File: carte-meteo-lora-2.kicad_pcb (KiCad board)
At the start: 4 copper layers, 50 x 50 mm, 79 parts, among them J1 USB_C_Receptacle_USB2.0_14P, J2 Conn_Coaxial, J3 Conn_Coaxial, J4 Conn_Coaxial, J5 Conn_01x04_Pin, SW1 SW_Push, SW2 SW_Push, U1 HS96L03W2C03, U2 SX1262TR8-GC, U3 LDL212PV33R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

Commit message: pcb: add uart routing
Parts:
- moved J5 7.89 mm to (128.8, 43.7), turned to 0 degrees
- moved R15 0.75 mm to (127.0, 40.2), turned to 90 degrees
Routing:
- net Net-(J5-Pin_4): track 0.00 -> 12.0 mm
- net /U0RXD: track 0.00 -> 10.6 mm
- net /U0TXD: track 0.00 -> 2.48 mm
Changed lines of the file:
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@@
 	(footprint "Resistor_SMD:R_0402_1005Metric"
 		(layer "F.Cu")
-		(at 126.975 41 180)
+		(at 126.975 40.25 90)
 		(descr "Resistor SMD 0402 (1005 Metric), square (rectangular) end terminal, IPC-7351 nominal, (Body size source: IPC-SM-782 page 72, https://www.pcb-3d.com/wordpress/wp-content/uploads/ipc-sm-782a_amendment_1_and_2.pdf)")
 		(tags "resistor")
 		(property "Reference" "R15"
-			(at 0 -1.17 0)
+			(at 0 -1.17 90)
 			(layer "F.SilkS")
 			(effects
@@
 		)
 		(property "Value" "470"
-			(at 0 1.17 0)
+			(at 0 1.17 90)
 			(layer "F.Fab")
 			(effects
@@
 		)
 		(property "Datasheet" ""
-			(at 0 0 0)
+			(at 0 0 90)
 			(layer "F.Fab")
 			(hide yes)
@@
 		)
 		(property "Description" "Resistor"
-			(at 0 0 0)
+			(at 0 0 90)
 			(layer "F.Fab")
 			(hide yes)
@@
 		)
 		(property "KiLib_Generator" "SMD_2terminal_chip_molded"
-			(at 0 0 0)
+			(at 0 0 90)
 			(layer "F.SilkS")
 			(hide yes)
@@
 		)
 		(property "Basic" "Y"
-			(at 0 0 180)
+			(at 0 0 90)
 			(unlocked yes)
 			(layer "F.Fab")
@@
 		)
 		(property "JLCPCB Part #" "C25117"
-			(at 0 0 180)
+			(at 0 0 90)
 			(unlocked yes)
 			(layer "F.Fab")
@@
 		)
 		(property "Manufacturer" "Uniroyal Elec"
-			(at 0 0 180)
+			(at 0 0 90)
 			(unlocked yes)
 			(layer "F.Fab")
@@
 		)
 		(property "Manufacturer Part Number" "0402WGF4700TCE"
-			(at 0 0 180)
+			(at 0 0 90)
 			(unlocked yes)
 			(layer "F.Fab")
@@
 		(duplicate_pad_numbers_are_jumpers no)
 		(fp_line
-			(start -0.153641 0.38)
-			(end 0.153641 0.38)
+			(start -0.153641 -0.38)
+			(end 0.153641 -0.38)
 			(stroke
 				(width 0.12)
@@
 		)
 		(fp_line
-			(start -0.153641 -0.38)
-			(end 0.153641 -0.38)
+			(start -0.153641 0.38)
+			(end 0.153641 0.38)
 			(stroke
 				(width 0.12)
@@
 		)
 		(fp_text user "${REFERENCE}"
-			(at 0 0 0)
+			(at 0 0 90)
 			(layer "F.Fab")
 			(effects
@@
 		)
 		(pad "1" smd roundrect
-			(at -0.51 0 180)
+			(at -0.51 0 90)
 			(size 0.54 0.64)
 			(layers "F.Cu" "F.Mask" "F.Paste")
@@
 		)
 		(pad "2" smd roundrect
-			(at 0.51 0 180)
+			(at 0.51 0 90)
 			(size 0.54 0.64)
 			(layers "F.Cu" "F.Mask" "F.Paste")
@@
 	(footprint "Connector_PinHeader_2.54mm:PinHeader_1x04_P2.54mm_Vertical"
 		(layer "F.Cu")
-		(at 128.75 51.56 180)
+		(at 128.75 43.67)
 		(descr "Through hole straight pin header, 1x04, 2.54mm pitch, single row")
 		(tags "Through hole pin header THT 1x04 2.54mm single row")
@@
 		(duplicate_pad_numbers_are_jumpers no)
 		(fp_line
-			(start 1.38 1.27)
-			(end 1.38 9)
+			(start -1.38 -1.38)
+			(end 0 -1.38)
 			(stroke
 				(width 0.12)
@@
 		)
 		(fp_line
-			(start -1.38 9)
-			(end 1.38 9)
+			(start -1.38 0)
+			(end -1.38 -1.38)
 			(stroke
 				(width 0.12)
@@
 		(fp_line
 			(start -1.38 1.27)
-			(end 1.38 1.27)
+			(end -1.38 9)
 			(stroke
 				(width 0.12)
@@
 		(fp_line
 			(start -1.38 1.27)
-			(end -1.38 9)
+			(end 1.38 1.27)
 			(stroke
 				(width 0.12)
@@
 		)
 		(fp_line
-			(start -1.38 0)
-			(end -1.38 -1.38)
+			(start -1.38 9)
+			(end 1.38 9)
 			(stroke
 				(width 0.12)
@@
 		)
 		(fp_line
-			(start -1.38 -1.38)
-			(end 0 -1.38)
+			(start 1.38 1.27)
+			(end 1.38 9)
 			(stroke
 				(width 0.12)
@@
 		)
 		(fp_line
-			(start 1.27 8.89)
-			(end -1.27 8.89)
+			(start -1.27 -0.635)
+			(end -0.635 -1.27)
 			(stroke
 				(width 0.1)
@@
 		)
 		(fp_line
-			(start 1.27 -1.27)
-			(end 1.27 8.89)
+			(start -1.27 8.89)
+			(end -1.27 -0.635)
 			(stroke
 				(width 0.1)
@@
 		)
 		(fp_line
-			(start -1.27 8.89)
-			(end -1.27 -0.635)
+			(start 1.27 -1.27)
+			(end 1.27 8.89)
 			(stroke
 				(width 0.1)
@@
 		)
 		(fp_line
-			(start -1.27 -0.635)
-			(end -0.635 -1.27)
+			(start 1.27 8.89)
+			(end -1.27 8.89)
 			(stroke
 				(width 0.1)
@@
 		)
 		(pad "1" thru_hole rect
-			(at 0 0 180)
+			(at 0 0)
 			(size 1.7 1.7)
 			(drill 1)
@@
 		)
 		(pad "2" thru_hole circle
-			(at 0 2.54 180)
+			(at 0 2.54)
 			(size 1.7 1.7)
 			(drill 1)
@@
 		)
 		(pad "3" thru_hole circle
-			(at 0 5.08 180)
+			(at 0 5.08)
 			(size 1.7 1.7)
 			(drill 1)
@@
 		)
 		(pad "4" thru_hole circle
-			(at 0 7.62 180)
+			(at 0 7.62)
 			(size 1.7 1.7)
 			(drill 1)
@@
 	)
 	(segment
+		(start 127.54 51.29)
+		(end 126.975 50.725)
+		(width 0.2)
+		(layer "F.Cu")
+		(net "Net-(J5-Pin_4)")
+	)
+	(segment
+		(start 128.75 51.29)
+		(end 127.54 51.29)
+		(width 0.2)
+		(layer "F.Cu")
+		(net "Net-(J5-Pin_4)")
+	)
+	(segment
+		(start 126.975 50.725)
+		(end 126.975 40.76)
+		(width 0.2)
+		(layer "F.Cu")
+		(net "Net-(J5-Pin_4)")
+	)
+	(segment
+		(start 126.49 39.74)
+		(end 125.4 38.65)
+		(width 0.2)
+		(layer "F.Cu")
+		(net "/U0TXD")
+	)
+	(segment
+		(start 126.975 39.74)
+		(end 126.49 39.74)
+		(width 0.2)
+		(layer "F.Cu")
+		(net "/U0TXD")
+	)
+	(segment
+		(start 125.4 38.65)
+		(end 124.95 38.65)
+		(width 0.2)
+		(layer "F.Cu")
+		(net "/U0TXD")
+	)
+	(segment
+		(start 127.25 38.75)
+		(end 127.545 39.045)
+		(width 0.2)
+		(layer "F.Cu")
+		(net "/U0RXD")
+	)
+	(segment
+		(start 124.95 38.25)
+		(end 125.75 38.25)
+		(width 0.2)
+		(layer "F.Cu")
+		(net "/U0RXD")
+	)
+	(segment
+		(start 127.545 39.045)
+		(end 127.545 45.005)
+		(width 0.2)
+		(layer "F.Cu")
+		(net "/U0RXD")
+	)
+	(segment
+		(start 126.25 38.75)
+		(end 127.25 38.75)
+		(width 0.2)
+		(layer "F.Cu")
+		(net "/U0RXD")
+	)
+	(segment
+		(start 125.75 38.25)
+		(end 126.25 38.75)
+		(width 0.2)
+		(layer "F.Cu")
+		(net "/U0RXD")
+	)
+	(segment
+		(start 127.545 45.005)
+		(end 128.75 46.21)
+		(width 0.2)
+		(layer "F.Cu")
+		(net "/U0RXD")
+	)
+	(segment

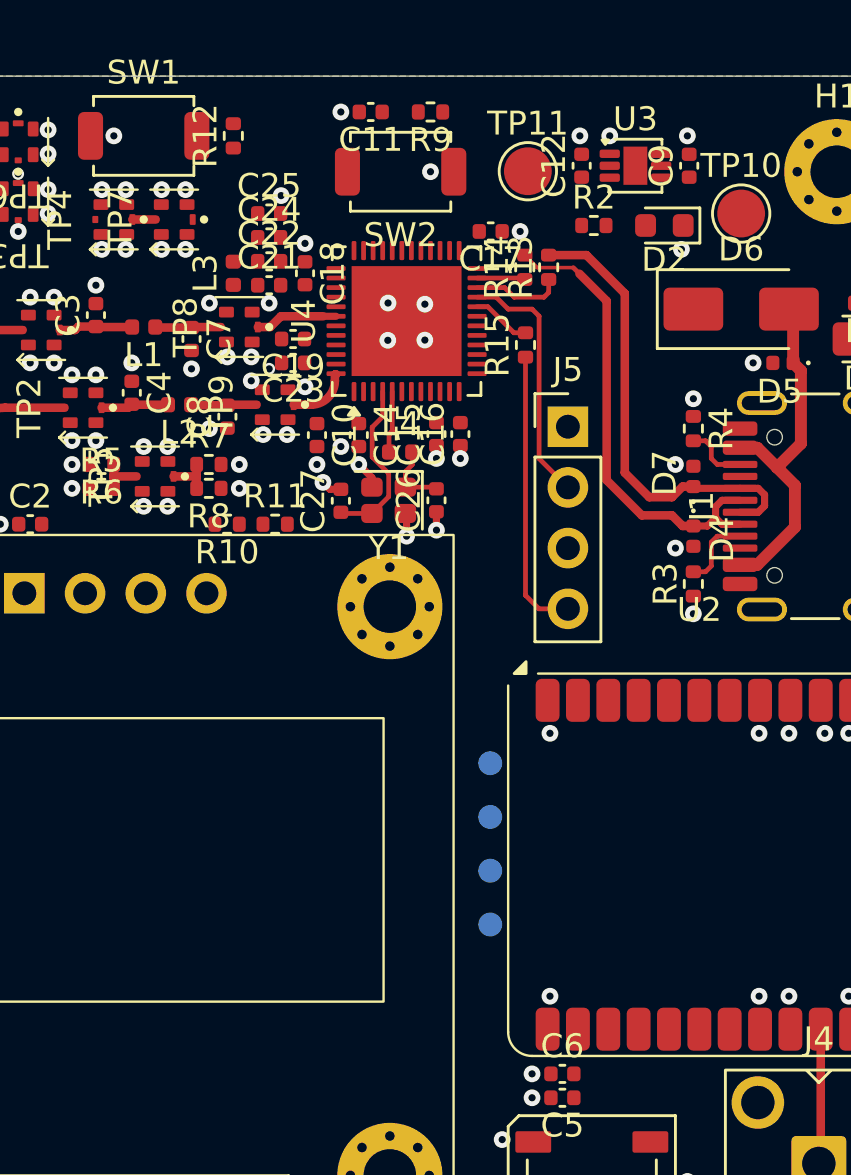
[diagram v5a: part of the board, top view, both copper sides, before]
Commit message: pcb: add i2c routing
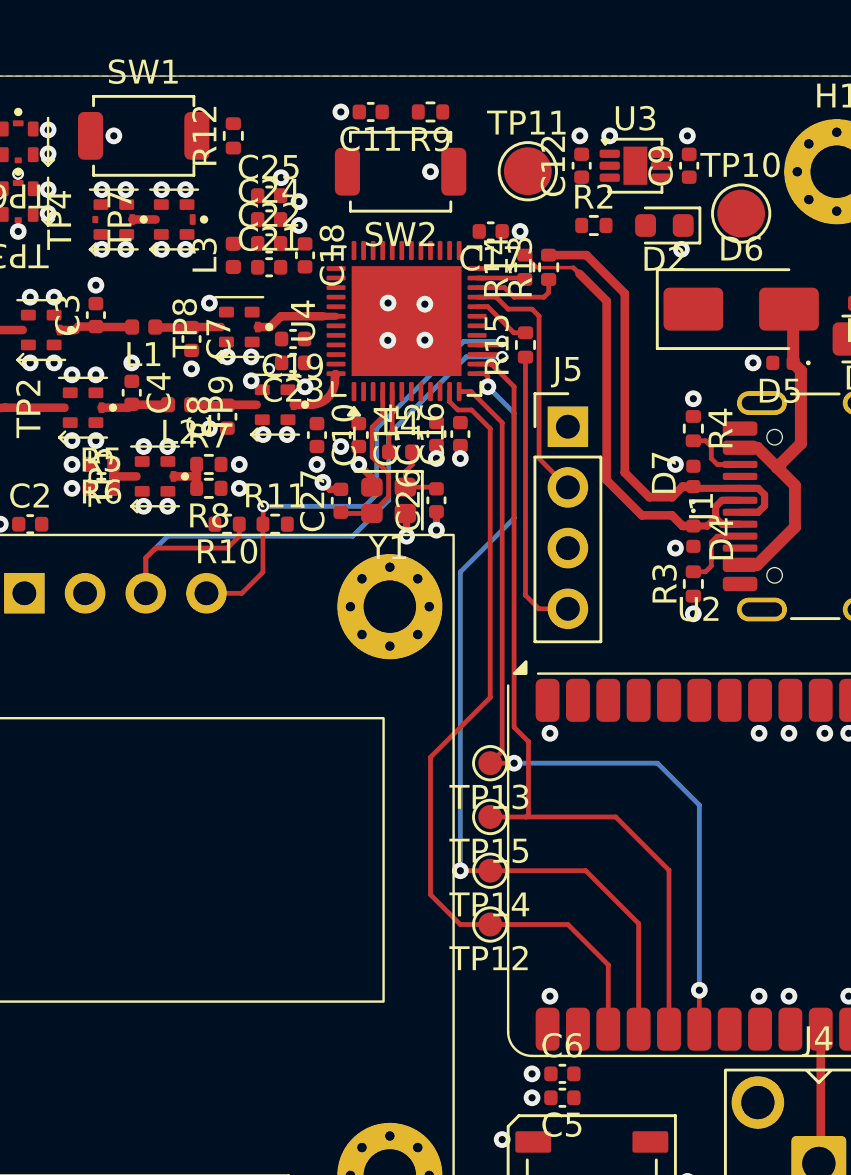
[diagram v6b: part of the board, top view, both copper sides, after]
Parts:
- TP12, TP13, TP14, TP15: moved to F.Cu
- moved C18 0.75 mm to (117.8, 36.5)
- moved C21 0.75 mm to (116.2, 37.0)
- moved C22 0.75 mm to (116.2, 36.0)
- moved C24 0.75 mm to (116.2, 35.0)
- moved C25 0.75 mm to (116.2, 34.0)
- moved L3 0.75 mm to (114.8, 36.5)
- turned TP12 to 180 degrees
- turned TP13 to 180 degrees
- turned TP14 to 180 degrees
- turned TP15 to 180 degrees
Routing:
- net /CS: track 0.00 -> 35.7 mm, vias 0 -> 2
- net /MISO: track 0.00 -> 35.4 mm, vias 0 -> 2
- net /MOSI: track 0.00 -> 35.3 mm
- net /SCK: track 0.00 -> 34.5 mm
- net /SCL: track 0.00 -> 28.8 mm, vias 0 -> 1
- net /SDA: track 0.00 -> 21.1 mm, vias 0 -> 2

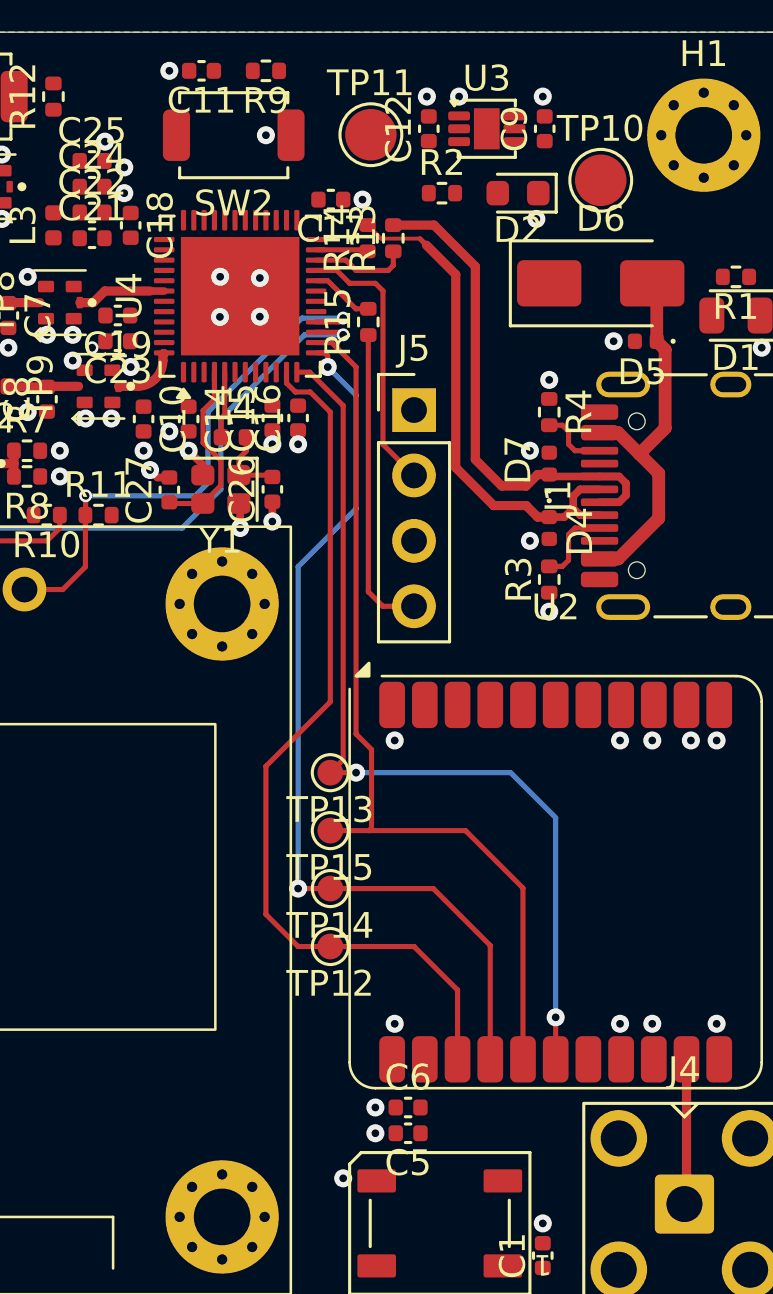
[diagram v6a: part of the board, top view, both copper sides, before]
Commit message: pcb: add lora module routing
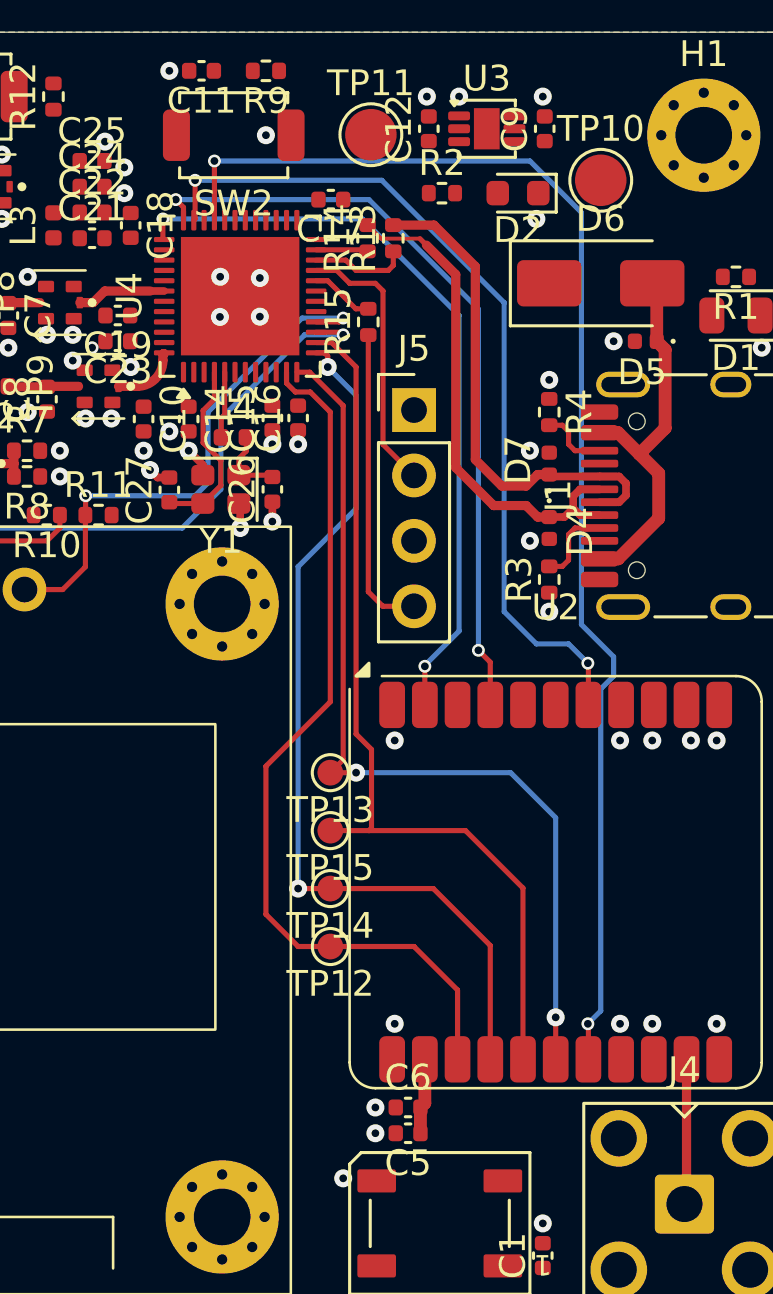
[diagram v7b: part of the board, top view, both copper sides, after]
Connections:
- U4 pad 17: /BUSY -> unconnected-(U4-GPIO8/SDIO_DATA0-Pad17)
- U4 pad 18: /DIO3 -> unconnected-(U4-GPIO9/SDIO_CLK-Pad18)
- U4 pad 19: /DIO1 -> unconnected-(U4-GPIO10/SDIO_CMD-Pad19)
- U4 pad 35: unconnected-(U4-GPIO25-Pad35) -> /DIO1
- U4 pad 36: unconnected-(U4-GPIO26-Pad36) -> /DIO3
- U4 pad 37: unconnected-(U4-GPIO27-Pad37) -> /BUSY
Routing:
- net /RST: track 0.00 -> 51.2 mm, vias 0 -> 2
- net /DIO1: track 0.00 -> 33.2 mm, vias 0 -> 2
- net /DIO3: track 0.00 -> 30.0 mm, vias 0 -> 2
- net /BUSY: track 0.00 -> 29.5 mm, vias 0 -> 2
- net +3V3: track 0.00 -> 2.94 mm
- net GND: vias 89 -> 88

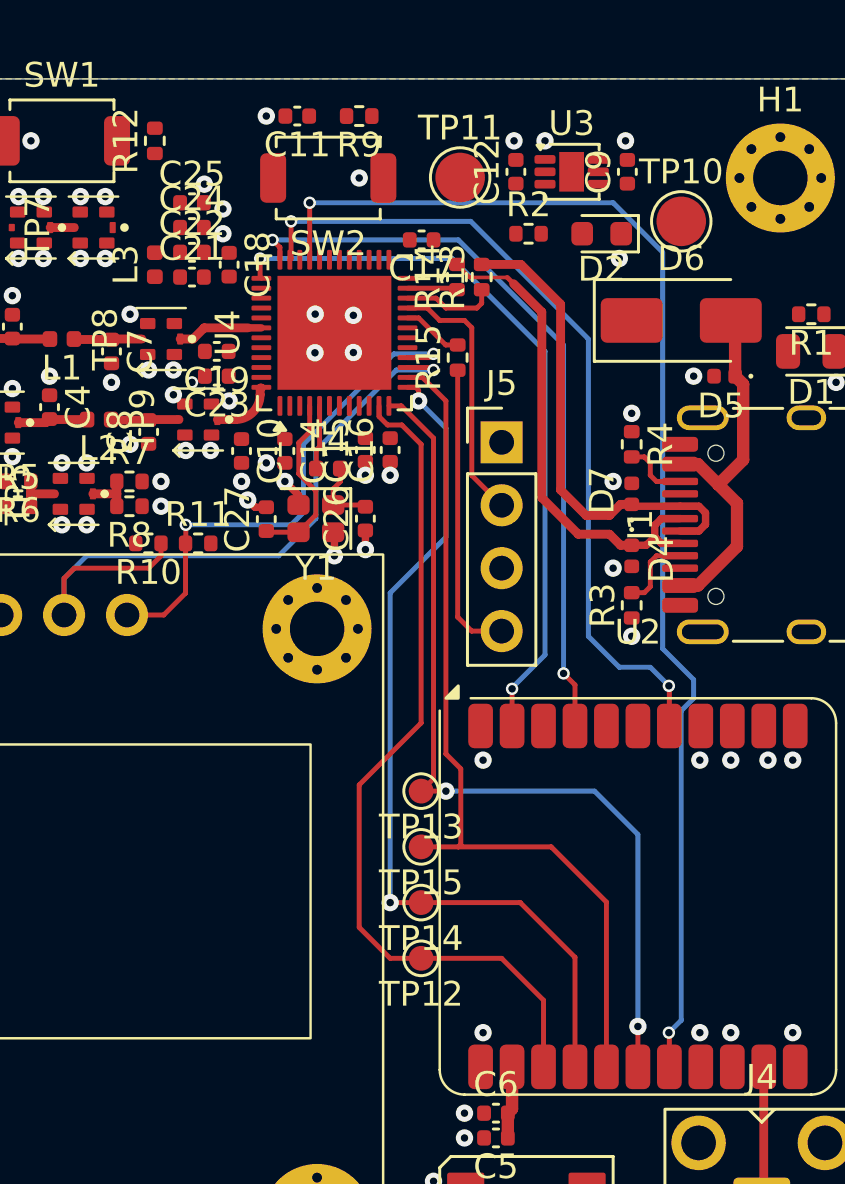
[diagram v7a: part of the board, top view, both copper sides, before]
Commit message: pcb: add +3v3 pwr routing
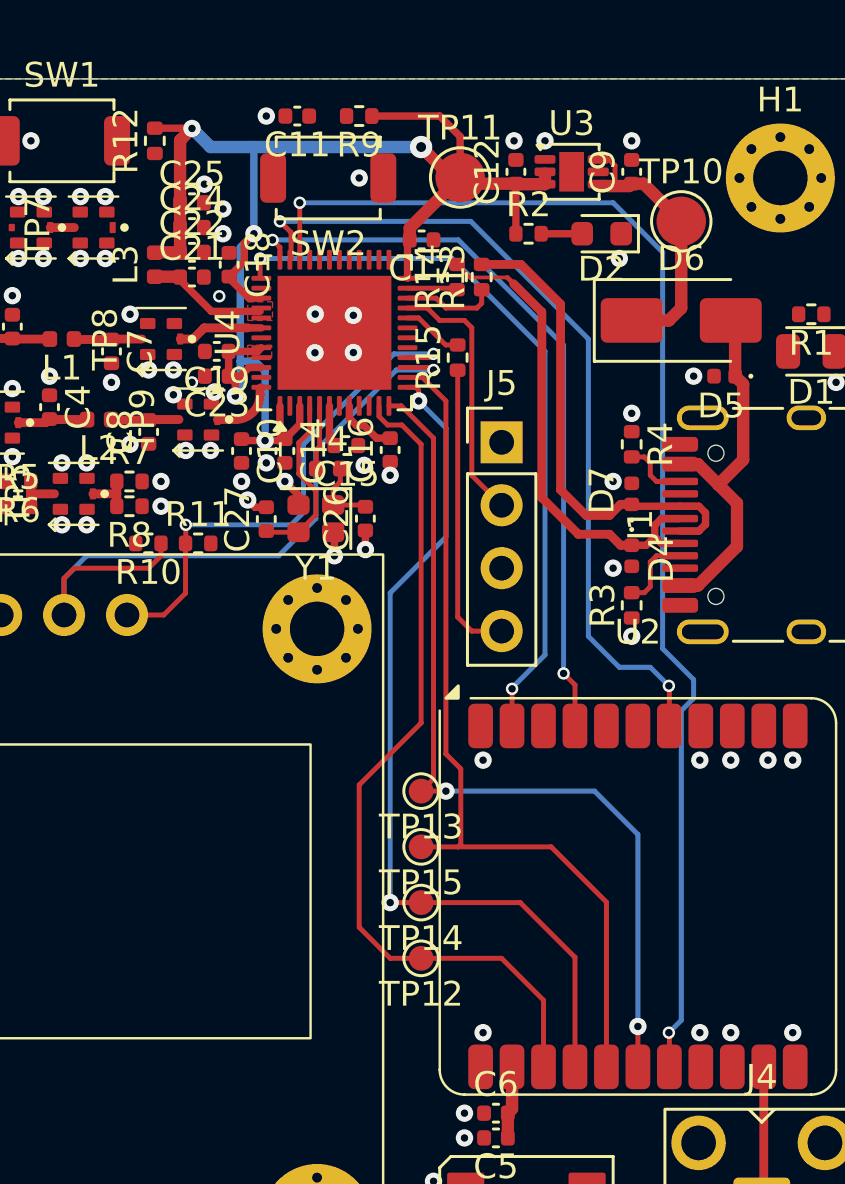
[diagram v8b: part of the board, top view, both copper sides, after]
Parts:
- moved C15 0.79 mm to (122.5, 43.8), turned to 180 degrees
- moved C9 0.18 mm to (134.0, 32.8)
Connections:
- U4 pad 33: /RST -> /RGB1
- U4 pad 34: /RGB1 -> /RST
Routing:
- net +3V3: track 2.94 -> 70.7 mm, vias 0 -> 5
- net +5V_MCU: track 0.00 -> 11.4 mm
- net Net-(U4-VDDA1): track 0.00 -> 4.90 mm
- net Net-(D2-A): track 0.00 -> 1.66 mm
- net /DIO1: track 33.2 -> 33.9 mm
- net GND: vias 88 -> 89
- added copper zone on F.Cu, net +3V3
- added copper zone on F.Cu, net Net-(U4-VDDA1)
